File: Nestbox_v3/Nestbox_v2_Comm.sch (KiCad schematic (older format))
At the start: 12 parts, among them J501 CONN_01X01, J502 CONN_01X06, Q501 NTR3A052PZT1G, U501 ESP-12S

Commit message: removed any unnecessary functions and connectors. corrected transistor bug
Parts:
- removed J501: CONN_01X01, Pin_Headers:Pin_Header_Straight_1x01_Pitch2.54mm, symbol CONN_01X01
- removed R502: 82k, Resistors_SMD:R_0603, symbol R
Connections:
- net +3V3: now also Q501.2 (S); no longer Q501.3 (D)
- net ESP12_VCC: now also Q501.3 (D); no longer Q501.2 (S)
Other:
- note removed: "!! PMOS IS INVERTED !!\n"
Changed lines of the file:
@@
 Text HLabel 2850 2950 0    60   Input ~ 0
 ESP12_ENABLE
-Text HLabel 6750 3900 0    60   Input ~ 0
-LORA_RST_N
-$Comp
-L R R502
-U 1 1 59FF56E8
-P 6900 3550
-F 0 "R502" H 6970 3596 50  0000 L CNN
-F 1 "82k" H 6970 3505 50  0000 L CNN
-F 2 "Resistors_SMD:R_0603" V 6830 3550 50  0001 C CNN
-F 3 "" H 6900 3550 50  0000 C CNN
-	1    6900 3550
-	1    0    0    -1
-$EndComp
-$Comp
-L +3.3V #PWR504
-U 1 1 59F64218
-P 6900 3400
-F 0 "#PWR504" H 6900 3250 50  0001 C CNN
-F 1 "+3.3V" H 6900 3540 50  0000 C CNN
-F 2 "" H 6900 3400 50  0000 C CNN
-F 3 "" H 6900 3400 50  0000 C CNN
-	1    6900 3400
-	1    0    0    -1
-$EndComp
-$Comp
-L CONN_01X01 J501
-U 1 1 5B144B9B
-P 7500 3900
-F 0 "J501" H 7500 4000 50  0000 C CNN
-F 1 "CONN_01X01" V 7600 3900 50  0000 C CNN
-F 2 "Pin_Headers:Pin_Header_Straight_1x01_Pitch2.54mm" H 7500 3900 50  0001 C CNN
-F 3 "" H 7500 3900 50  0001 C CNN
-	1    7500 3900
-	1    0    0    -1
-$EndComp
 $Comp
 L R R505
@@
 Wire Wire Line
 	3700 5600 4050 5600
-Connection ~ 6900 3900
-Wire Wire Line
-	6900 3900 6900 3700
-Wire Wire Line
-	6750 3900 7300 3900
 Wire Wire Line
 	3700 6000 4550 6000
@@
 F 3 "" H 3200 2950 50  0001 C CNN
 	1    3200 2950
-	1    0    0    -1
+	1    0    0    1
 $EndComp
 $Comp
@@
 	1    0    0    -1
 $EndComp
-Text Notes 2450 2150 0    118  ~ 0
-!! PMOS IS INVERTED !!\n
 $EndSCHEMATC

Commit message: exchanged both inductor footprints.
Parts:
- R501, R503, R504, R505, R506: value 10K -> 10k
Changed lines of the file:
@@
 P 2550 5300
 F 0 "R501" H 2620 5346 50  0000 L CNN
-F 1 "10K" H 2620 5255 50  0000 L CNN
+F 1 "10k" H 2620 5255 50  0000 L CNN
 F 2 "Resistors_SMD:R_0603" V 2480 5300 50  0001 C CNN
 F 3 "" H 2550 5300 50  0000 C CNN
@@
 P 4400 5750
 F 0 "R505" H 4470 5796 50  0000 L CNN
-F 1 "10K" H 4470 5705 50  0000 L CNN
+F 1 "10k" H 4470 5705 50  0000 L CNN
 F 2 "Resistors_SMD:R_0603" V 4330 5750 50  0001 C CNN
 F 3 "" H 4400 5750 50  0000 C CNN
@@
 P 2150 5300
 F 0 "R503" H 2220 5346 50  0000 L CNN
-F 1 "10K" H 2220 5255 50  0000 L CNN
+F 1 "10k" H 2220 5255 50  0000 L CNN
 F 2 "Resistors_SMD:R_0603" V 2080 5300 50  0001 C CNN
 F 3 "" H 2150 5300 50  0000 C CNN
@@
 P 4550 5750
 F 0 "R506" H 4620 5796 50  0000 L CNN
-F 1 "10K" H 4620 5705 50  0000 L CNN
+F 1 "10k" H 4620 5705 50  0000 L CNN
 F 2 "Resistors_SMD:R_0603" V 4480 5750 50  0001 C CNN
 F 3 "" H 4550 5750 50  0000 C CNN
@@
 P 4000 6100
 F 0 "R504" H 4070 6146 50  0000 L CNN
-F 1 "10K" H 4070 6055 50  0000 L CNN
+F 1 "10k" H 4070 6055 50  0000 L CNN
 F 2 "Resistors_SMD:R_0603" V 3930 6100 50  0001 C CNN
 F 3 "" H 4000 6100 50  0000 C CNN

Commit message: added MPN for all components for PCBA
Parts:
- Q501: MPN (none) -> NTR3A052PZT1G
- R501, R503, R504, R505, R506: MPN (none) -> RC0603JR-0710KL
- R507: MPN (none) -> RC0603FR-0782KL
- U501: MPN (none) -> ESP-12F
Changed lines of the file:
@@
-EESchema Schematic File Version 2
+EESchema Schematic File Version 4
 LIBS:power
 LIBS:device
@@
 LIBS:contrib
 LIBS:valves
-LIBS:Octanis3
 LIBS:Nestbox_v2-cache
-EELAYER 25 0
+EELAYER 26 0
 EELAYER END
 $Descr A4 11693 8268
@@
 F 2 "Octanis3:ESP-12E_SMD_UART_ONLY" H 2800 5050 60  0001 C CNN
 F 3 "" H 2800 5050 60  0001 C CNN
+F 4 "ESP-12F" H 0   0   50  0001 C CNN "MPN"
 	1    2800 5050
 	1    0    0    -1
@@
 F 2 "Resistors_SMD:R_0603" V 2480 5300 50  0001 C CNN
 F 3 "" H 2550 5300 50  0000 C CNN
+F 4 "RC0603JR-0710KL" H 0   0   50  0001 C CNN "MPN"
 	1    2550 5300
 	1    0    0    -1
@@
 F 2 "Resistors_SMD:R_0603" V 4330 5750 50  0001 C CNN
 F 3 "" H 4400 5750 50  0000 C CNN
+F 4 "RC0603JR-0710KL" H 0   0   50  0001 C CNN "MPN"
 	1    4400 5750
 	1    0    0    -1
@@
 F 2 "Resistors_SMD:R_0603" V 2080 5300 50  0001 C CNN
 F 3 "" H 2150 5300 50  0000 C CNN
+F 4 "RC0603JR-0710KL" H 0   0   50  0001 C CNN "MPN"
 	1    2150 5300
 	1    0    0    -1
@@
 F 2 "Resistors_SMD:R_0603" V 4480 5750 50  0001 C CNN
 F 3 "" H 4550 5750 50  0000 C CNN
+F 4 "RC0603JR-0710KL" H 0   0   50  0001 C CNN "MPN"
 	1    4550 5750
 	1    0    0    -1
@@
 F 2 "Resistors_SMD:R_0603" V 3930 6100 50  0001 C CNN
 F 3 "" H 4000 6100 50  0000 C CNN
+F 4 "RC0603JR-0710KL" H 0   0   50  0001 C CNN "MPN"
 	1    4000 6100
 	0    1    1    0
@@
 F 2 "TO_SOT_Packages_SMD:TSOT-23" H 3400 3050 50  0001 C CNN
 F 3 "" H 3200 2950 50  0001 C CNN
+F 4 "NTR3A052PZT1G" H 0   0   50  0001 C CNN "MPN"
 	1    3200 2950
 	1    0    0    1
@@
 F 2 "Resistors_SMD:R_0603" V 2880 2750 50  0001 C CNN
 F 3 "" H 2950 2750 50  0000 C CNN
+F 4 "RC0603FR-0782KL" H 0   0   50  0001 C CNN "MPN"
 	1    2950 2750
 	1    0    0    -1

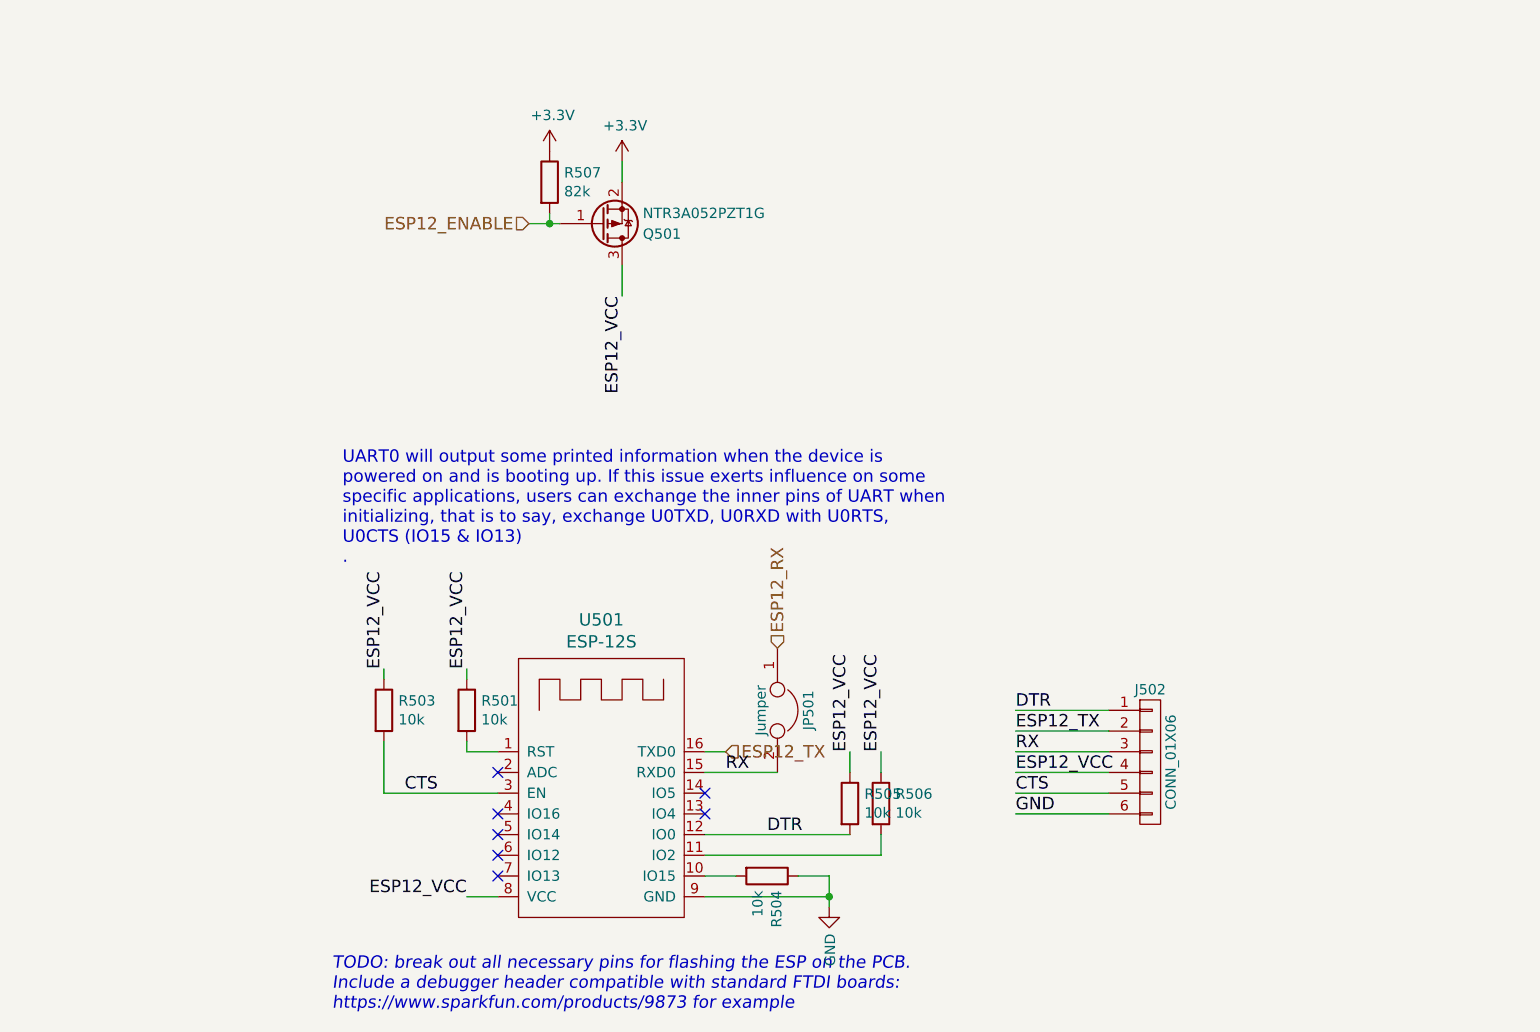
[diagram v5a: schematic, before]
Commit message: production status nestbox v3
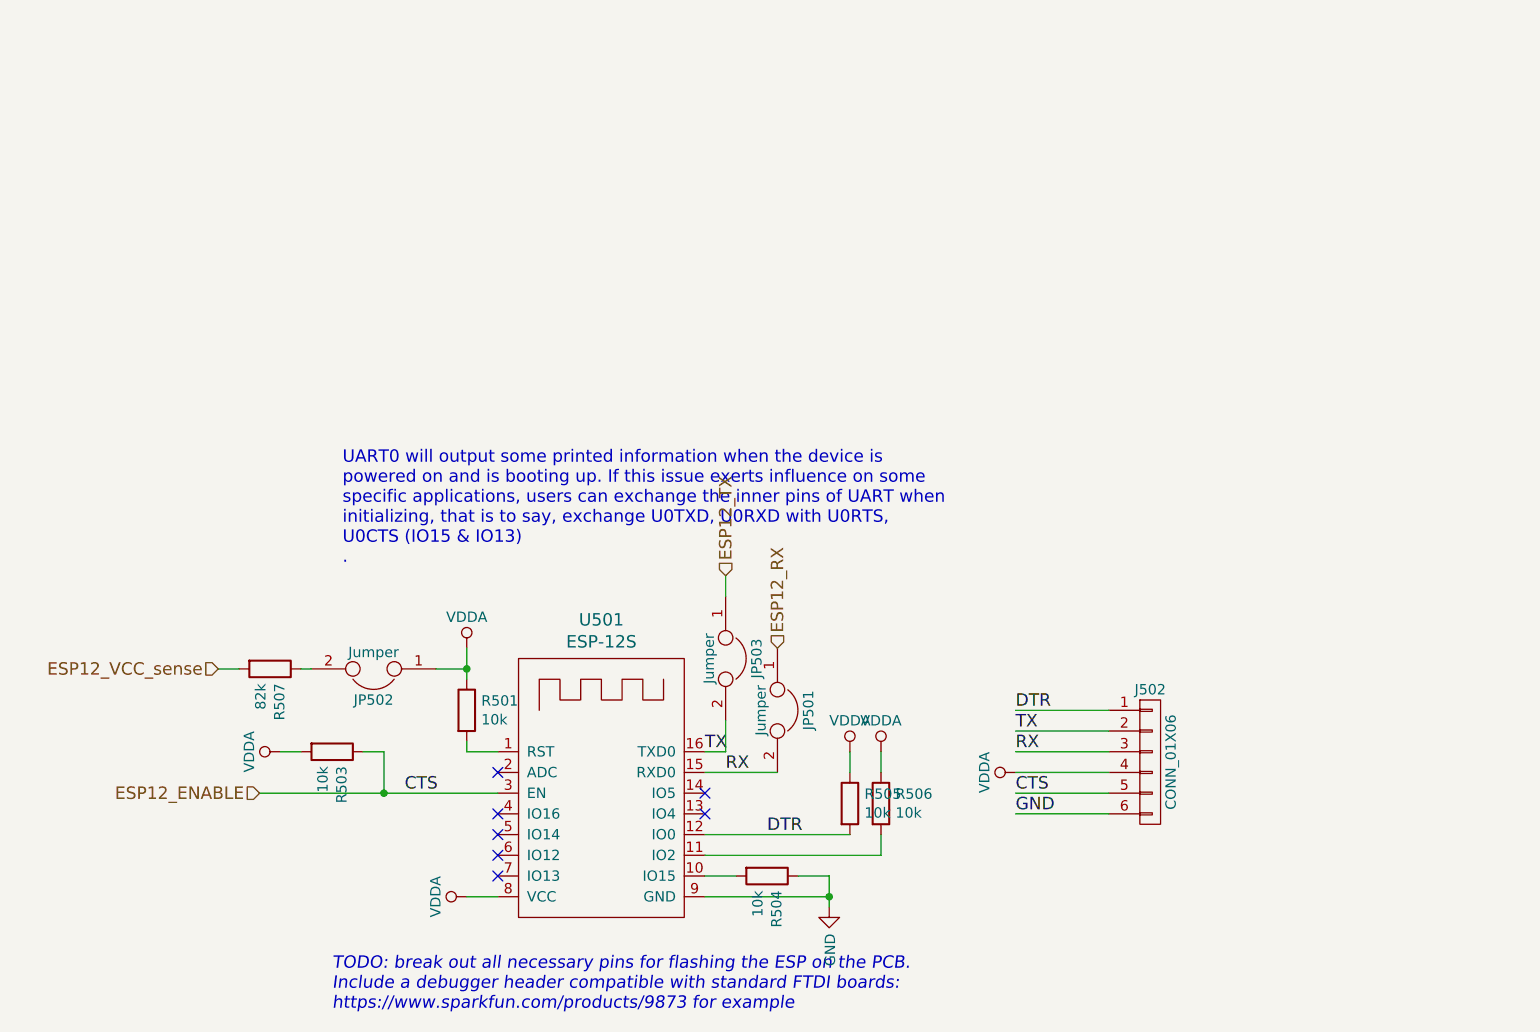
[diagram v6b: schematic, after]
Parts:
- removed Q501: NTR3A052PZT1G, TO_SOT_Packages_SMD:TSOT-23, symbol Q_PMOS_GSD
- added JP502, JP503: Jumper, Connect:GS2, symbol Jumper
- R507: MPN RC0603FR-0782KL -> RC0603JR-0710KL
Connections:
- net ESP12_ENABLE: now also J502.5 (P5), R503.1, U501.3 (EN); no longer R507.2
- net ESP12_TX: now also JP503.1; no longer J502.2 (P2), U501.16 (TXD0)
- net +3V3: no longer names the net of R507.1
- net +3V3: now also JP502.2
- removed net CTS: J502.5 (P5), R503.2, U501.3 (EN)
- net ESP12_VCC renamed VDDA
- net VDDA: now also R503.2, JP502.1; no longer R503.1
- new net ESP12_VCC_sense: R507.2
- new net TX: J502.2 (P2), JP503.2, U501.16 (TXD0)
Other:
- moved on the sheet: R503
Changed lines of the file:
@@
 $EndComp
 $Comp
-L GND #PWR047
+L GND #PWR052
 U 1 1 59FF60B0
 P 4300 6250
-F 0 "#PWR047" H 4300 6000 50  0001 C CNN
+F 0 "#PWR052" H 4300 6000 50  0001 C CNN
 F 1 "GND" V 4305 6122 50  0000 R CNN
 F 2 "" H 4300 6250 50  0000 C CNN
@@
 Text Notes 1950 4600 0    60   ~ 0
 UART0 will output some printed information when the device is \npowered on and is booting up. If this issue exerts influence on some \nspecific applications, users can exchange the inner pins of UART when \ninitializing, that is to say, exchange U0TXD, U0RXD with U0RTS, \nU0CTS (IO15 & IO13)\n.
-Text HLabel 3800 5500 2    60   Input ~ 0
+Text HLabel 3800 4650 1    60   Input ~ 0
 ESP12_TX
 Text HLabel 4050 5000 1    60   Input ~ 0
 ESP12_RX
-Text HLabel 2850 2950 0    60   Input ~ 0
+Text HLabel 1550 5700 0    60   Input ~ 0
 ESP12_ENABLE
 $Comp
@@
 $EndComp
 $Comp
-L +3.3V #PWR048
-U 1 1 5B158F7F
-P 3300 2650
-F 0 "#PWR048" H 3300 2500 50  0001 C CNN
-F 1 "+3.3V" H 3315 2823 50  0000 C CNN
-F 2 "" H 3300 2650 50  0000 C CNN
-F 3 "" H 3300 2650 50  0000 C CNN
-	1    3300 2650
-	1    0    0    -1
-$EndComp
-$Comp
 L R R503
 U 1 1 5B1595E2
-P 2150 5300
-F 0 "R503" H 2220 5346 50  0000 L CNN
-F 1 "10k" H 2220 5255 50  0000 L CNN
-F 2 "Resistors_SMD:R_0603" V 2080 5300 50  0001 C CNN
-F 3 "" H 2150 5300 50  0000 C CNN
-F 4 "RC0603JR-0710KL" H 0   0   50  0001 C CNN "MPN"
-	1    2150 5300
-	1    0    0    -1
+P 1900 5500
+F 0 "R503" H 1970 5546 50  0000 L CNN
+F 1 "10k" H 1970 5455 50  0000 L CNN
+F 2 "Resistors_SMD:R_0603" V 1830 5500 50  0001 C CNN
+F 3 "" H 1900 5500 50  0000 C CNN
+F 4 "RC0603JR-0710KL" H -250 200 50  0001 C CNN "MPN"
+	1    1900 5500
+	0    1    1    0
 $EndComp
 $Comp
@@
 Text Label 5200 5300 0    60   ~ 0
 DTR
-Text Label 5200 5400 0    60   ~ 0
-ESP12_TX
 Text Label 5200 5500 0    60   ~ 0
 RX
-Text Label 5200 5600 0    60   ~ 0
-ESP12_VCC
-Text Label 5200 5700 0    60   ~ 0
-CTS
 Text Label 5200 5800 0    60   ~ 0
 GND
-Text Label 4550 5500 1    60   ~ 0
-ESP12_VCC
-Text Label 4400 5500 1    60   ~ 0
-ESP12_VCC
-Text Label 2550 5100 1    60   ~ 0
-ESP12_VCC
-Text Label 2150 5100 1    60   ~ 0
-ESP12_VCC
-Text Label 2250 5700 0    60   ~ 0
-CTS
 Text Label 4000 5900 0    60   ~ 0
 DTR
-Text Label 3300 3300 3    60   ~ 0
-ESP12_VCC
 $Comp
 L R R506
@@
 $EndComp
 Wire Wire Line
-	2550 5100 2550 5150
+	2550 5000 2550 5150
 Wire Wire Line
 	2550 5450 2550 5500
@@
 Connection ~ 4300 6200
 Wire Wire Line
-	2150 5100 2150 5150
-Wire Wire Line
 	5650 5300 5200 5300
 Wire Wire Line
@@
 Wire Wire Line
 	5650 5800 5200 5800
-Wire Wire Line
-	2150 5450 2150 5700
-Wire Wire Line
-	2150 5700 2700 5700
-Wire Wire Line
-	2850 2950 3000 2950
-Wire Wire Line
-	3300 2750 3300 2650
-Wire Wire Line
-	3300 3300 3300 3150
 $Comp
 L R R504
@@
 Text Label 3800 5600 0    60   ~ 0
 RX
-Text Label 2550 6200 2    60   ~ 0
-ESP12_VCC
-$Comp
-L Q_PMOS_GSD Q501
-U 1 1 5B18B1E8
-P 3200 2950
-F 0 "Q501" H 3400 3000 50  0000 L CNN
-F 1 "NTR3A052PZT1G" H 3400 2900 50  0000 L CNN
-F 2 "TO_SOT_Packages_SMD:TSOT-23" H 3400 3050 50  0001 C CNN
-F 3 "" H 3200 2950 50  0001 C CNN
-F 4 "NTR3A052PZT1G" H 0   0   50  0001 C CNN "MPN"
-	1    3200 2950
-	1    0    0    1
-$EndComp
+Text Label 2250 5700 0    60   ~ 0
+CTS
+Text Label 5200 5700 0    60   ~ 0
+CTS
 $Comp
 L R R507
-U 1 1 5B28C223
-P 2950 2750
-F 0 "R507" H 3020 2796 50  0000 L CNN
-F 1 "82k" H 3020 2705 50  0000 L CNN
-F 2 "Resistors_SMD:R_0603" V 2880 2750 50  0001 C CNN
-F 3 "" H 2950 2750 50  0000 C CNN
-F 4 "RC0603FR-0782KL" H 0   0   50  0001 C CNN "MPN"
-	1    2950 2750
-	1    0    0    -1
-$EndComp
-Wire Wire Line
-	2950 2900 2950 2950
-Connection ~ 2950 2950
-$Comp
-L +3.3V #PWR049
-U 1 1 5B28C2B7
-P 2950 2600
-F 0 "#PWR049" H 2950 2450 50  0001 C CNN
-F 1 "+3.3V" H 2965 2773 50  0000 C CNN
-F 2 "" H 2950 2600 50  0000 C CNN
-F 3 "" H 2950 2600 50  0000 C CNN
-	1    2950 2600
-	1    0    0    -1
-$EndComp
+U 1 1 5BF52201
+P 1600 5100
+F 0 "R507" H 1670 5146 50  0000 L CNN
+F 1 "82k" H 1670 5055 50  0000 L CNN
+F 2 "Resistors_SMD:R_0603" V 1530 5100 50  0001 C CNN
+F 3 "" H 1600 5100 50  0000 C CNN
+F 4 "RC0603JR-0710KL" H -550 -200 50  0001 C CNN "MPN"
+	1    1600 5100
+	0    1    1    0
+$EndComp
+Connection ~ 2550 5100
+Wire Wire Line
+	1450 5100 1350 5100
+Text HLabel 1350 5100 0    60   Input ~ 0
+ESP12_VCC_sense
+Wire Wire Line
+	1750 5100 1800 5100
+Wire Wire Line
+	2400 5100 2550 5100
+$Comp
+L Jumper JP502
+U 1 1 5BF54615
+P 2100 5100
+F 0 "JP502" H 2100 5250 50  0000 C CNN
+F 1 "Jumper" H 2100 5020 50  0000 C CNN
+F 2 "Connect:GS2" H 2100 5100 50  0001 C CNN
+F 3 "" H 2100 5100 50  0001 C CNN
+	1    2100 5100
+	-1   0    0    1
+$EndComp
+$Comp
+L VDDA #PWR053
+U 1 1 5BF57845
+P 2550 5000
+F 0 "#PWR053" H 2550 4850 50  0001 C CNN
+F 1 "VDDA" H 2550 5150 50  0000 C CNN
+F 2 "" H 2550 5000 50  0001 C CNN
+F 3 "" H 2550 5000 50  0001 C CNN
+	1    2550 5000
+	1    0    0    -1
+$EndComp
+$Comp
+L VDDA #PWR054
+U 1 1 5BF57875
+P 4400 5500
+F 0 "#PWR054" H 4400 5350 50  0001 C CNN
+F 1 "VDDA" H 4400 5650 50  0000 C CNN
+F 2 "" H 4400 5500 50  0001 C CNN
+F 3 "" H 4400 5500 50  0001 C CNN
+	1    4400 5500
+	1    0    0    -1
+$EndComp
+$Comp
+L VDDA #PWR055
+U 1 1 5BF5789E
+P 4550 5500
+F 0 "#PWR055" H 4550 5350 50  0001 C CNN
+F 1 "VDDA" H 4550 5650 50  0000 C CNN
+F 2 "" H 4550 5500 50  0001 C CNN
+F 3 "" H 4550 5500 50  0001 C CNN
+	1    4550 5500
+	1    0    0    -1
+$EndComp
+$Comp
+L VDDA #PWR056
+U 1 1 5BF57938
+P 5200 5600
+F 0 "#PWR056" H 5200 5450 50  0001 C CNN
+F 1 "VDDA" H 5200 5750 50  0000 C CNN
+F 2 "" H 5200 5600 50  0001 C CNN
+F 3 "" H 5200 5600 50  0001 C CNN
+	1    5200 5600
+	0    -1   -1   0
+$EndComp
+$Comp
+L VDDA #PWR057
+U 1 1 5BF57A01
+P 2550 6200
+F 0 "#PWR057" H 2550 6050 50  0001 C CNN
+F 1 "VDDA" H 2550 6350 50  0000 C CNN
+F 2 "" H 2550 6200 50  0001 C CNN
+F 3 "" H 2550 6200 50  0001 C CNN
+	1    2550 6200
+	0    -1   -1   0
+$EndComp
+$Comp
+L VDDA #PWR058
+U 1 1 5BF583A6
+P 1650 5500
+F 0 "#PWR058" H 1650 5350 50  0001 C CNN
+F 1 "VDDA" H 1650 5650 50  0000 C CNN
+F 2 "" H 1650 5500 50  0001 C CNN
+F 3 "" H 1650 5500 50  0001 C CNN
+	1    1650 5500
+	0    -1   -1   0
+$EndComp
+Wire Wire Line
+	1650 5500 1750 5500
+Wire Wire Line
+	2050 5500 2150 5500
+Wire Wire Line
+	2150 5500 2150 5700
+Connection ~ 2150 5700
+Wire Wire Line
+	1550 5700 2700 5700
+$Comp
+L Jumper JP503
+U 1 1 5BF5CB9A
+P 3800 5050
+F 0 "JP503" H 3800 5200 50  0000 C CNN
+F 1 "Jumper" H 3800 4970 50  0000 C CNN
+F 2 "Connect:GS2" H 3800 5050 50  0001 C CNN
+F 3 "" H 3800 5050 50  0001 C CNN
+	1    3800 5050
+	0    1    1    0
+$EndComp
+Wire Wire Line
+	3800 4650 3800 4750
+Wire Wire Line
+	3800 5350 3800 5500
+Text Label 5200 5400 0    60   ~ 0
+TX
+Text Label 3700 5500 0    60   ~ 0
+TX
 $EndSCHEMATC
